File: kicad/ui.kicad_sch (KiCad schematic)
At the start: 4 parts, among them U3 Pico, U9 SN75176BP

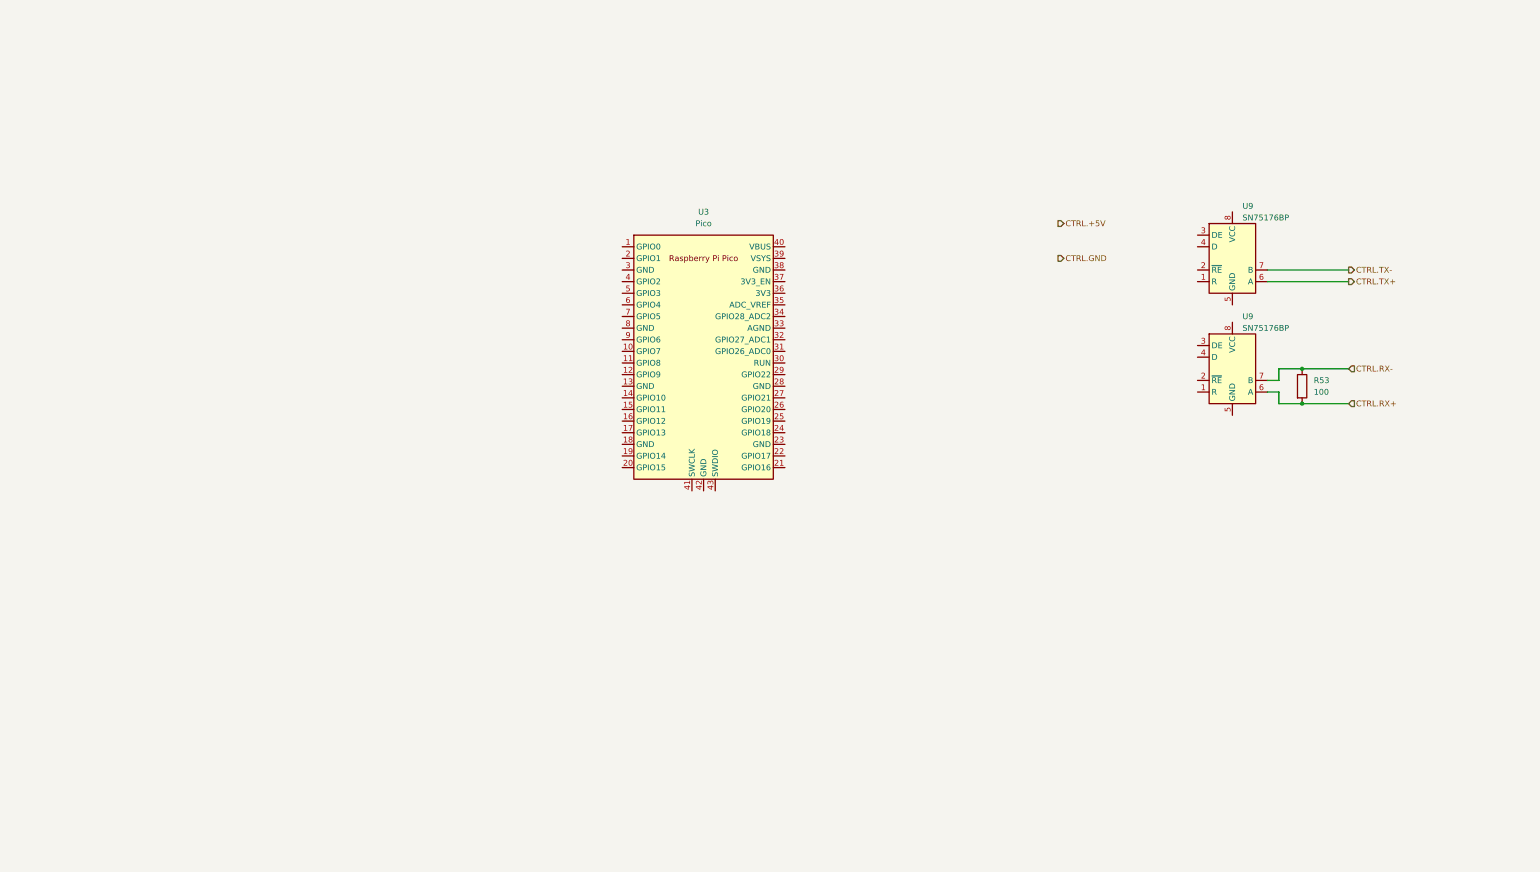
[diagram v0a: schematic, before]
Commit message: Add kibot config
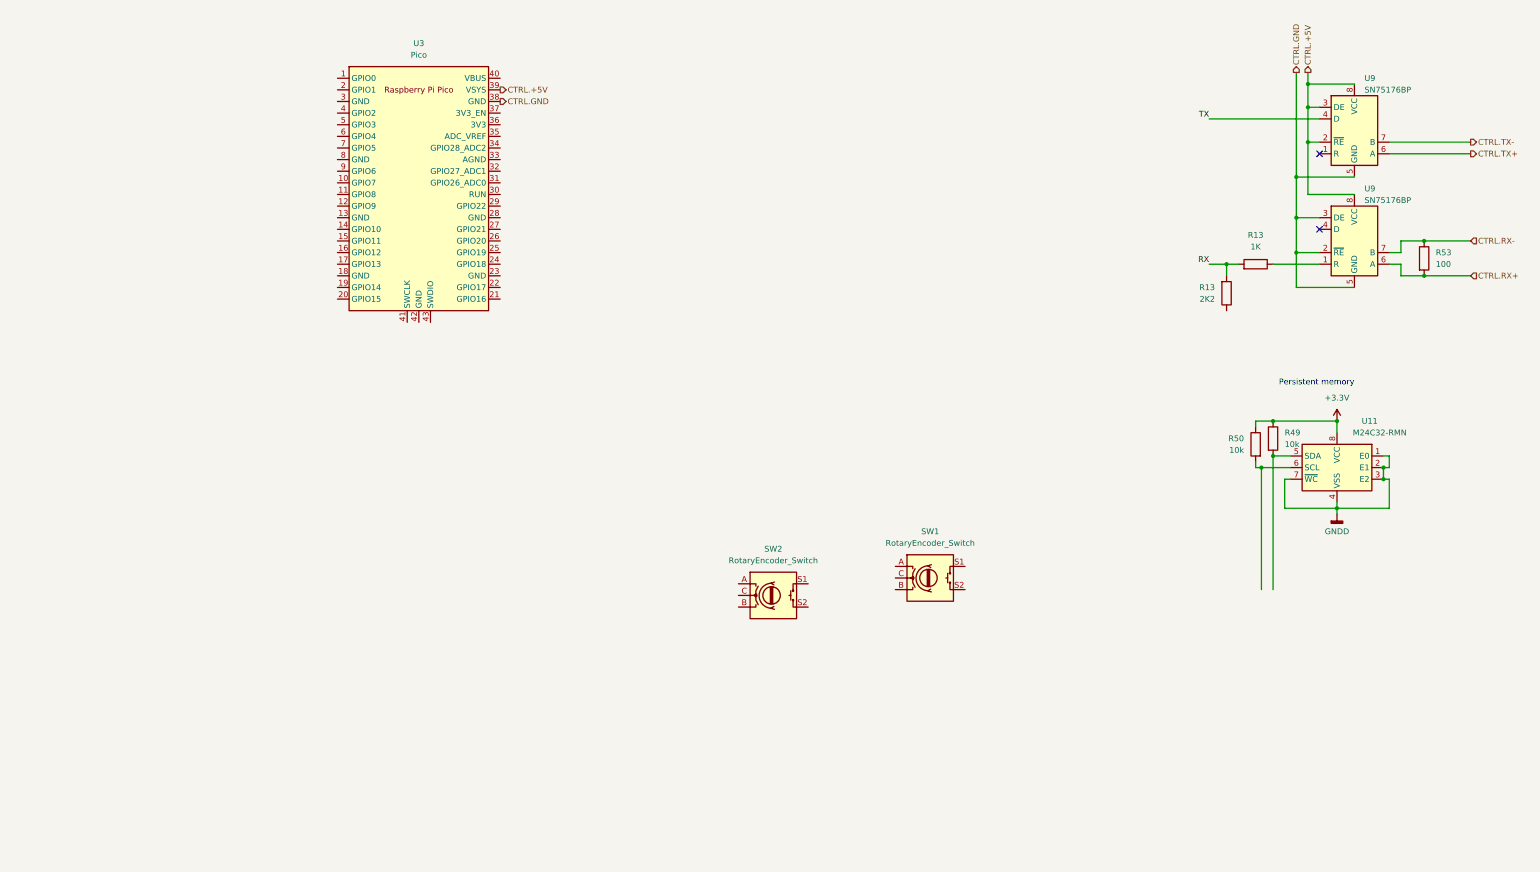
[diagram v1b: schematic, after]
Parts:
- added R13: 2K2, Resistor_THT:R_Axial_DIN0207_L6.3mm_D2.5mm_P7.62mm_Horizontal, symbol Device:R
- added R13: 1K, Resistor_THT:R_Axial_DIN0207_L6.3mm_D2.5mm_P7.62mm_Horizontal, symbol Device:R
- added R49, R50: 10k, Resistor_THT:R_Axial_DIN0207_L6.3mm_D2.5mm_P7.62mm_Horizontal, symbol Device:R
- added SW1, SW2: RotaryEncoder_Switch, Rotary_Encoder:RotaryEncoder_Bourns_Vertical_PEC12R-3xxxF-Sxxxx, symbol Device:RotaryEncoder_Switch
- added U11: M24C32-RMN, Package_SO:SOIC-8_3.9x4.9mm_P1.27mm, symbol Memory_EEPROM:M24C02-RMN
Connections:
- net CTRL.+5V: now also U3.39 (VSYS), U9.2 (~{RE}), U9.3 (DE), U9.8 (VCC), U9.8 (VCC)
- net CTRL.GND: now also U3.38 (GND), U9.2 (~{RE}), U9.3 (DE), U9.5 (GND), U9.5 (GND)
- net TX: now reaches U9.4 (D)
- net at U9.1 (R): now also R13.1
- new net: R50.2, U11.6 (SCL)
- new net: R49.2, U11.5 (SDA)
- new net +3.3V: R49.1, R50.1, U11.8 (VCC)
- new net GNDD: U11.1 (E0), U11.2 (E1), U11.3 (E2), U11.4 (VSS), U11.7 (~{WC})
- new net RX: R13.2, R13.2
- no-connect marks 0 -> 2
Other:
- note added: "Persistent memory"
- moved on the sheet: R53, U3, U9

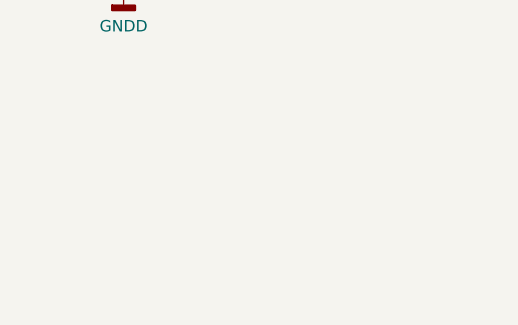
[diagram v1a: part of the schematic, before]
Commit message: Separate boards automatically
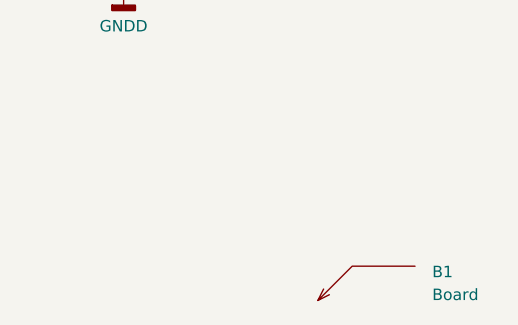
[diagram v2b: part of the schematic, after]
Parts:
- added B1: Board, PCM_kikit:Board, symbol PCM_kikit:Board
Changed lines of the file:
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@@
+    )
+  )
+  (symbol (lib_id "PCM_kikit:Board") (at 260.35 157.48 0) (unit 1)
+    (in_bom no) (on_board yes) (dnp no) (fields_autoplaced)
+    (property "Reference" "B1" (at 273.05 154.305 0)
+      (effects (font (size 1.27 1.27)) (justify left))
+    )
+    (property "Value" "Board" (at 273.05 156.845 0)
+      (effects (font (size 1.27 1.27)) (justify left))
+    )
+    (property "Footprint" "PCM_kikit:Board" (at 270.51 156.845 0)
+      (effects (font (size 1.27 1.27)) hide)
+    )
+    (property "Datasheet" "" (at 260.35 157.48 0)
+      (effects (font (size 1.27 1.27)) hide)
+    )
+    (instances
+      (project "digipsu"
+        (path "/ec5fec7a-fde3-4f44-b689-61159deeeb72/a0108b83-e991-42ef-8684-1d1a6fe91cd6"
+          (reference "B1") (unit 1)
+        )
+        (path "/ec5fec7a-fde3-4f44-b689-61159deeeb72/4943d487-6290-480b-b97a-e25fc46bcb0d"
+          (reference "B2") (unit 1)
+        )
+      )
     )
   )

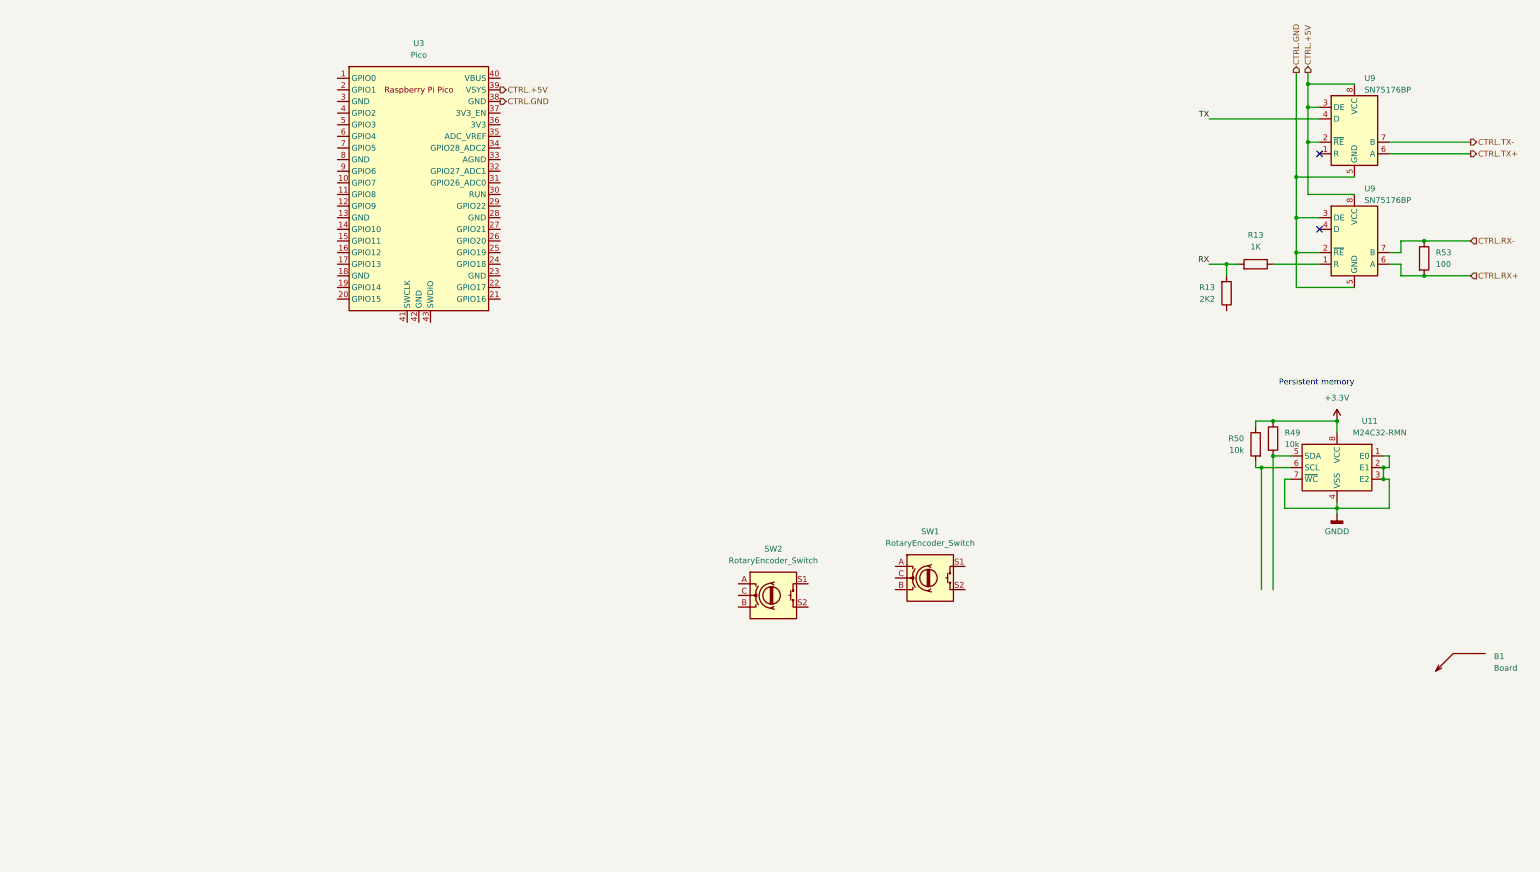
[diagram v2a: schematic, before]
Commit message: Add latest changes to fix CI
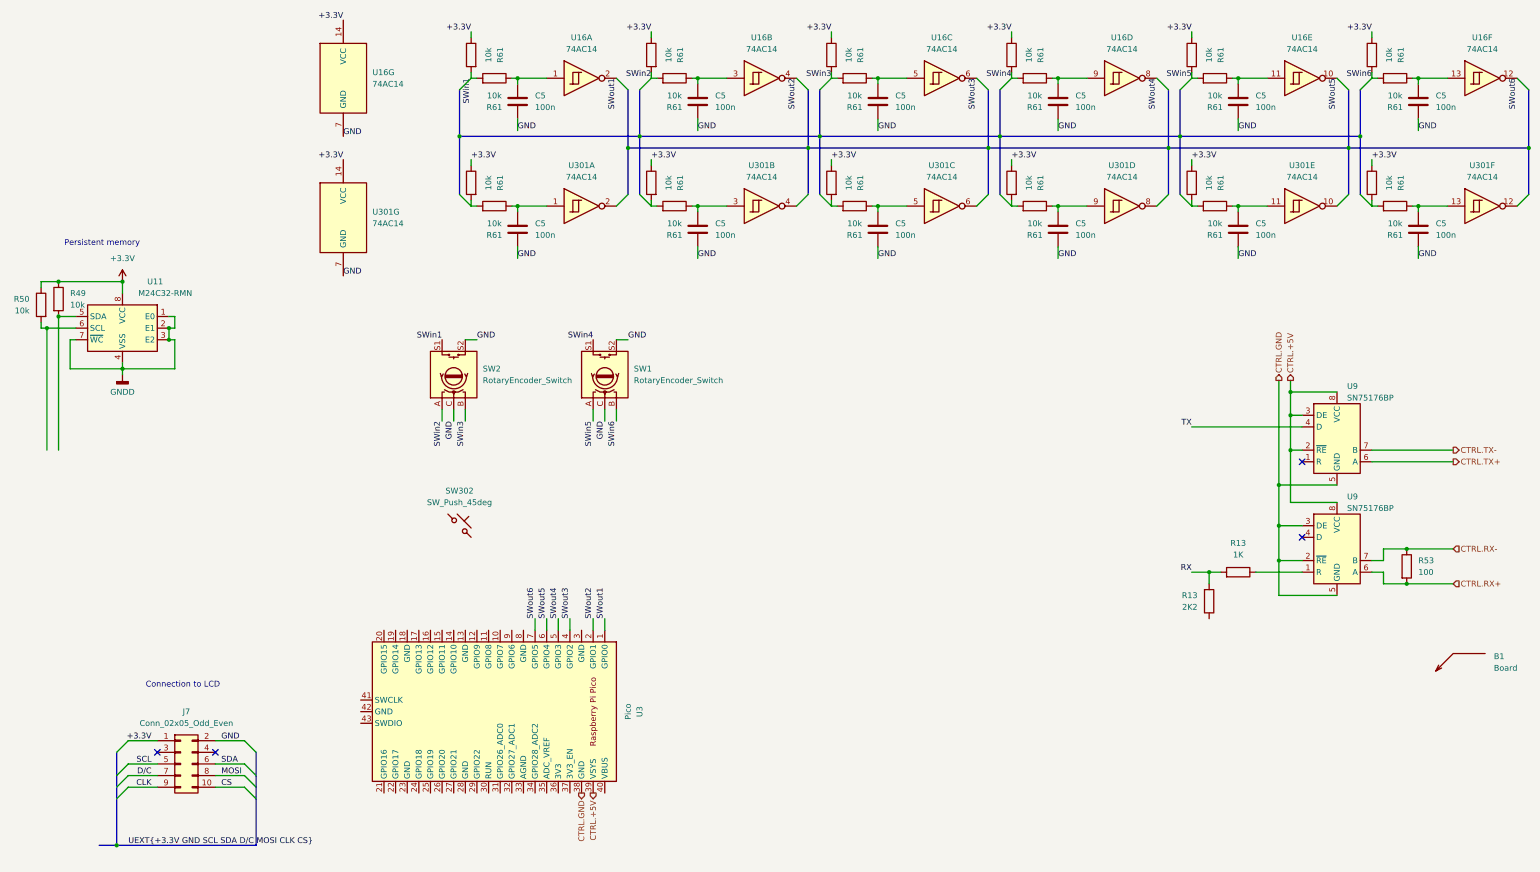
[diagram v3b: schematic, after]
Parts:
- added C5 (x12): 100n, Capacitor_THT:C_Disc_D3.8mm_W2.6mm_P2.50mm, symbol Device:C
- added J7: Conn_02x05_Odd_Even, symbol Connector_Generic:Conn_02x05_Odd_Even
- added R61 (x24): 10k, Resistor_THT:R_Axial_DIN0207_L6.3mm_D2.5mm_P7.62mm_Horizontal, symbol Device:R
- added SW302: SW_Push_45deg, symbol Switch:SW_Push_45deg
- added U16, U301: 74AC14, Package_SO:SOIC-14_3.9x8.7mm_P1.27mm, symbol 74xx:74HC14
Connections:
- net +3.3V: now also J7.1 (Pin_1), R61.1, R61.1, R61.1, R61.1, R61.1, R61.1, R61.1, R61.1, R61.1, R61.1, R61.1, R61.1, U16.14 (VCC), U301.14 (VCC)
- net SWin5: now reaches SW1.A
- net SWin5: now also R61.2, R61.2
- net SWin6: now reaches SW1.B
- net SWin6: now also R61.2, R61.2
- net GND: now reaches SW1.C
- net GND: now also SW1.S2, SW2.C, SW2.S2, C5.2, C5.2, C5.2, C5.2, C5.2, C5.2, C5.2, C5.2, C5.2, C5.2, C5.2, C5.2, J7.2 (Pin_2), U16.7 (GND), U301.7 (GND)
- net SWin4: now reaches SW1.S1
- net SWin4: now also R61.2, R61.2
- net SWout1: now reaches U3.1 (GPIO0)
- net SWout1: now also U16.2
- net SWout2: now reaches U3.2 (GPIO1)
- net SWout2: now also U16.4
- net SWout3: now reaches U3.4 (GPIO2)
- net SWout3: now also U16.6
- net SWout4: now reaches U3.5 (GPIO3)
- net SWout4: now also U16.8
- net SWout5: now reaches U3.6 (GPIO4)
- net SWout5: now also U16.10
- net SWout6: now reaches U3.7 (GPIO5)
- net SWout6: now also U16.12
- net SWin2: now reaches SW2.A
- net SWin2: now also R61.2, R61.2
- net SWin3: now reaches SW2.B
- net SWin3: now also R61.2, R61.2
- net SWin1: now reaches SW2.S1
- net SWin1: now also R61.2, R61.2
- new net: C5.1, R61.1, U16.11
- new net: R61.2, R61.2 (x6)
- new net: C5.1, R61.1, U16.13
- new net: C5.1, R61.1, U301.3
- new net: C5.1, R61.1, U16.1
- new net: C5.1, R61.1, U301.11
- new net: C5.1, R61.1, U16.5
- new net: C5.1, R61.1, U301.1
- new net: C5.1, R61.1, U301.5
- new net: C5.1, R61.1, U16.9
- new net: C5.1, R61.1, U16.3
- new net: C5.1, R61.1, U301.9
- new net: C5.1, R61.1, U301.13
- new net CLK: J7.9 (Pin_9)
- new net CS: J7.10 (Pin_10)
- new net D/C: J7.7 (Pin_7)
- new net MOSI: J7.8 (Pin_8)
- new net SCL: J7.5 (Pin_5)
- new net SDA: J7.6 (Pin_6)
- no-connect marks 2 -> 4
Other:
- note added: "Connection to LCD"
- moved on the sheet: R13, R49, R50, R53, SW1, SW2, U11, U3, U9
